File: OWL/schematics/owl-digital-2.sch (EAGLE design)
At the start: 72 parts, among them IC1 LMC6482, IC10 IS42S16400J, IC4 CS4271, IC8 STM32F756ZLQFP144, IC9 N25Q128A13, U2 1uH, U3 1uH, U4 V_REG_LM3940IMP, Y1 24.576MHz, Y3 25MHz

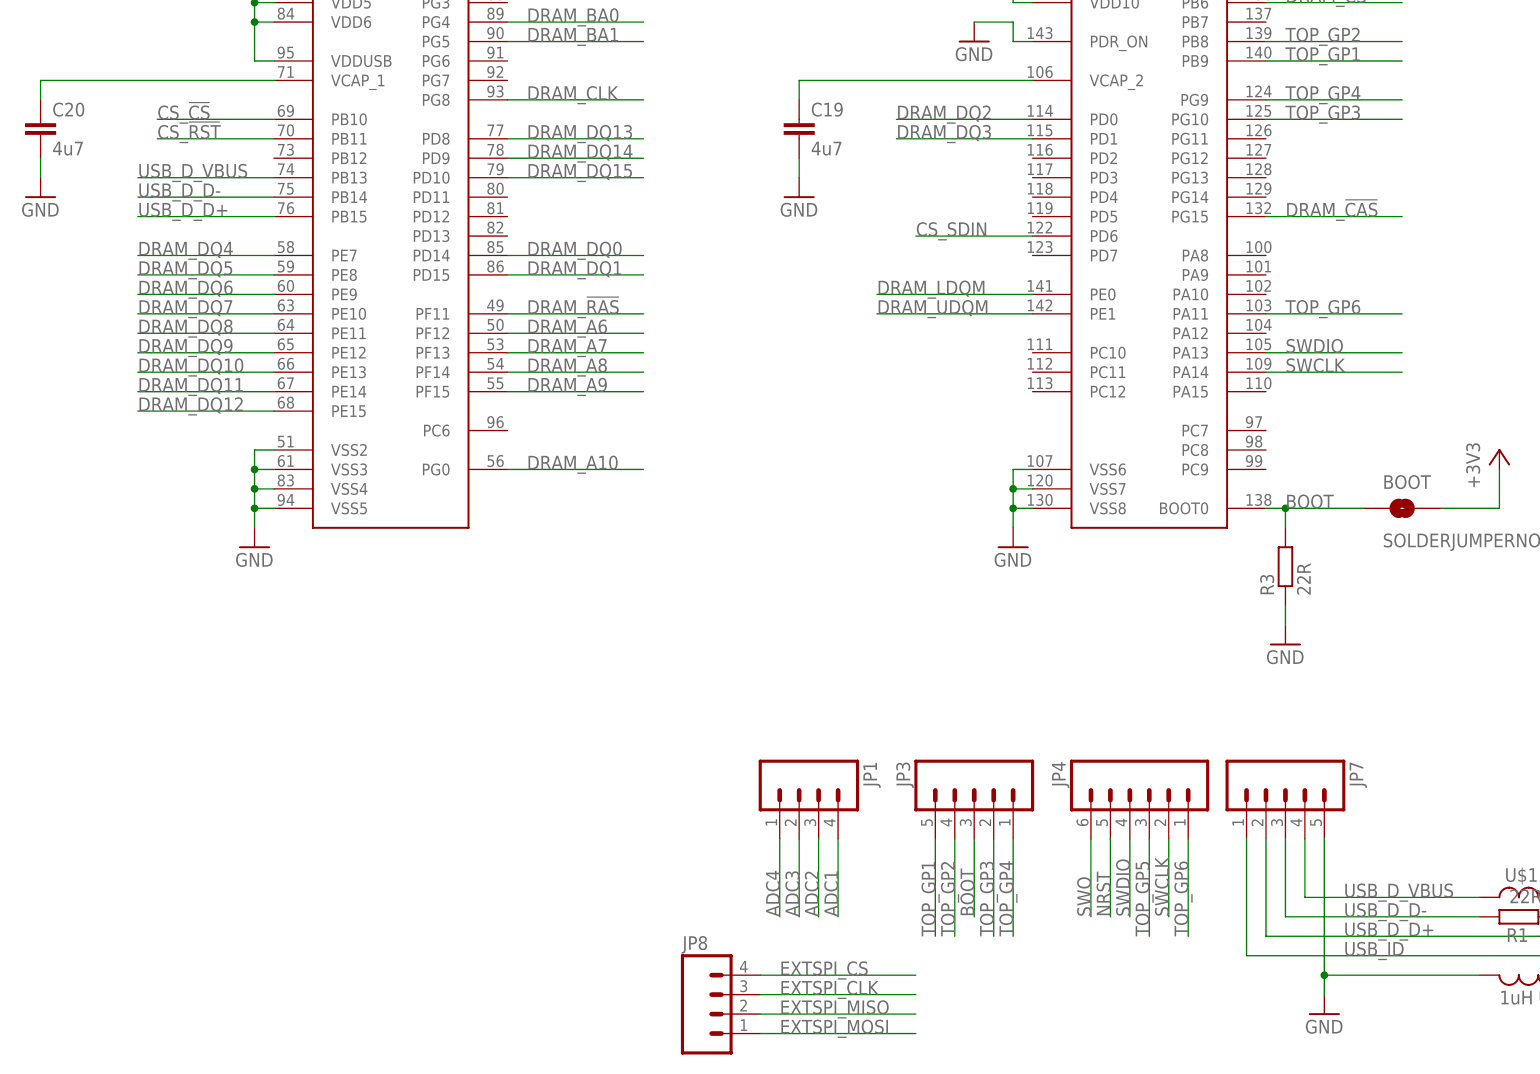
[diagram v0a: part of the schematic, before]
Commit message: updated USB ID pin on cube file and hardware
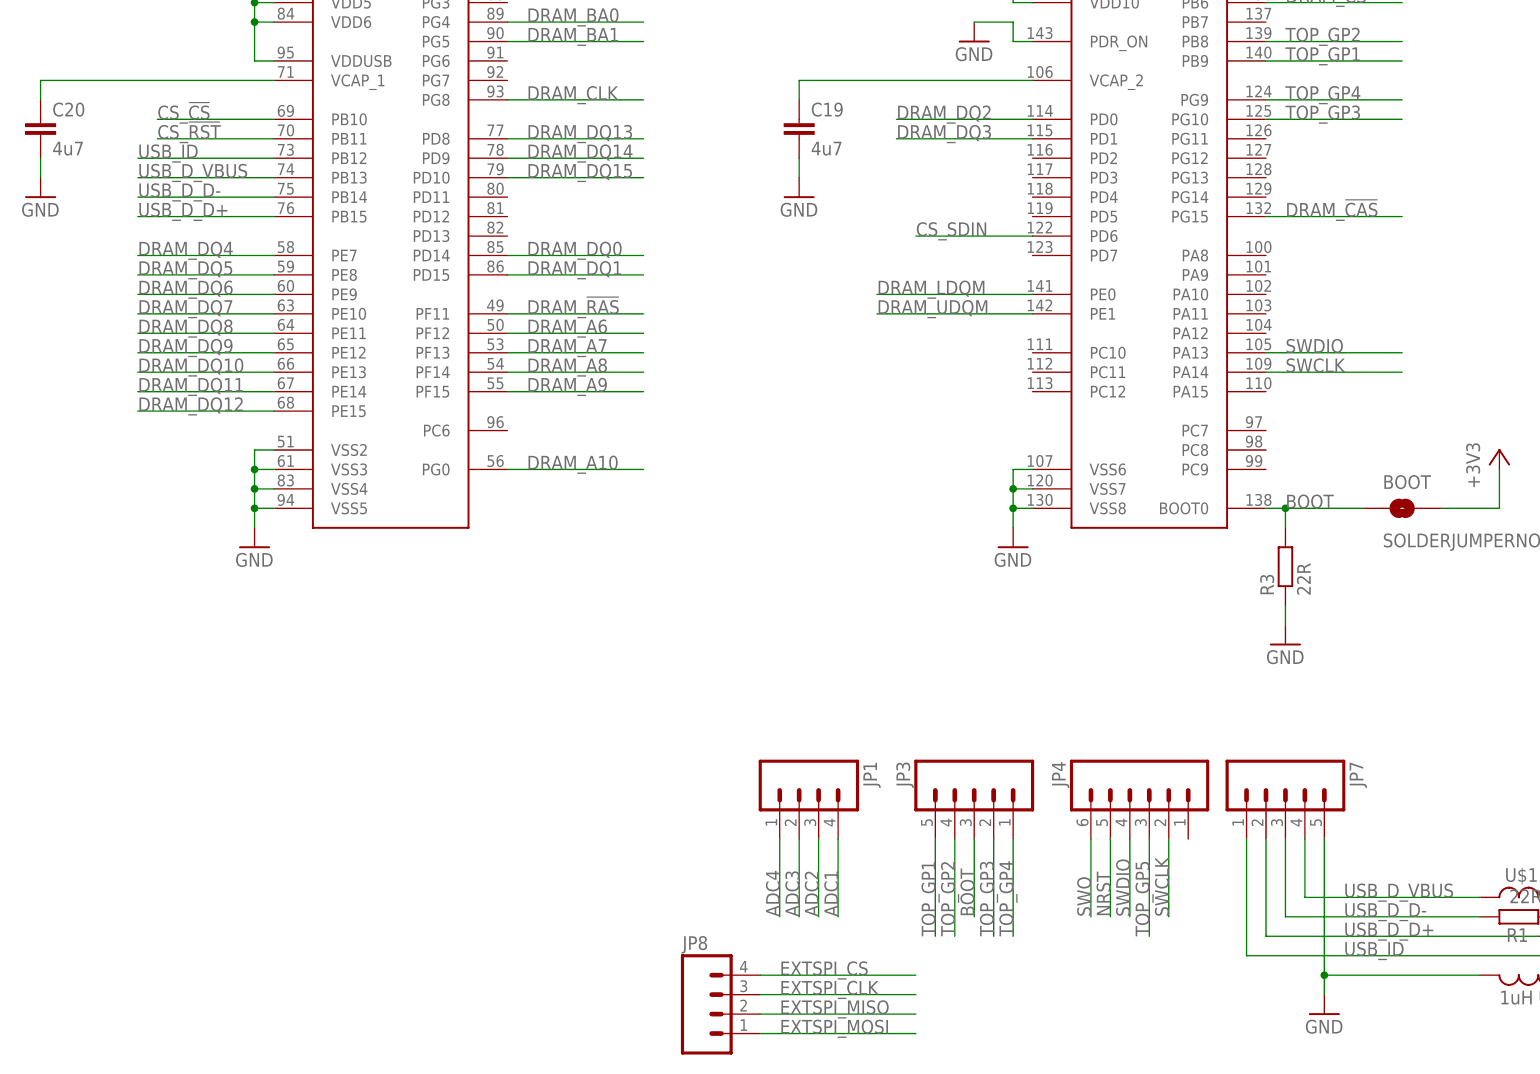
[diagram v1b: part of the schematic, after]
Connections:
- removed net TOP_GP6: IC8G$3.PA11, JP4.1
- net USB_ID: now also IC8G$2.PB12
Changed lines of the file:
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@@
 <pinref part="USB1" gate="USB" pin="ID"/>
+</segment>
+<segment>
+<pinref part="IC8" gate="G$2" pin="PB12"/>
+<wire x1="139.7" y1="119.38" x2="121.92" y2="119.38" width="0.1524" layer="91"/>
+<label x="121.92" y="119.38" size="1.778" layer="95"/>
 </segment>
 </net>
@@
 </segment>
 </net>
-<net name="TOP_GP6" class="0">
-<segment>
-<pinref part="JP4" gate="G$1" pin="1"/>
-<wire x1="259.08" y1="30.48" x2="259.08" y2="17.78" width="0.1524" layer="91"/>
-<label x="259.08" y="17.78" size="1.778" layer="95" rot="R90"/>
-</segment>
-<segment>
-<pinref part="IC8" gate="G$3" pin="PA11"/>
-<wire x1="269.24" y1="99.06" x2="287.02" y2="99.06" width="0.1524" layer="91"/>
-<label x="271.78" y="99.06" size="1.778" layer="95"/>
-</segment>
-</net>

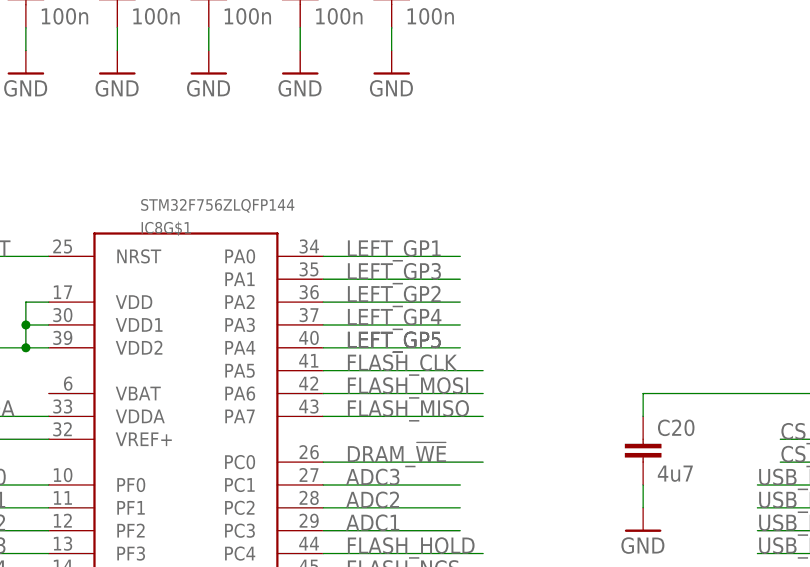
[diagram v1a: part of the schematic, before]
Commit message: Created cube file for Tesseract and swapped GP1 & GP3 pins on OWL digital v2
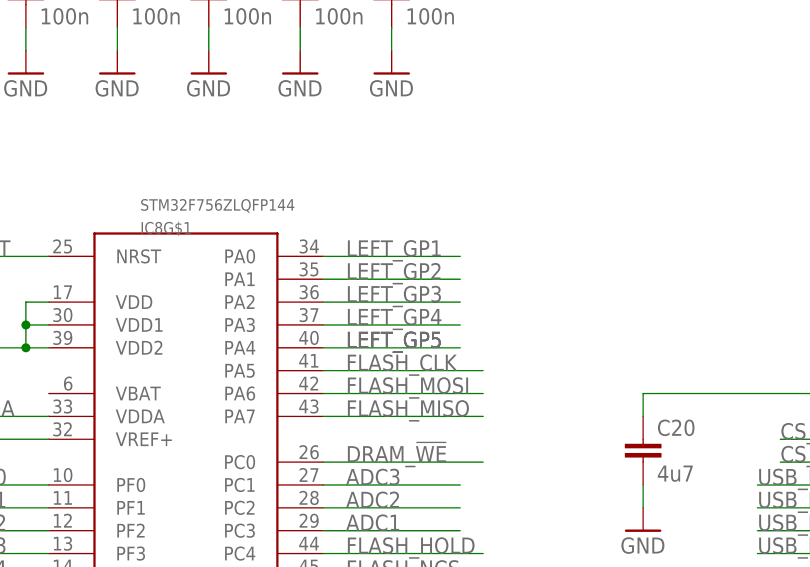
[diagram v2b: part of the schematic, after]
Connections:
- net LEFT_GP2: now also IC8G$1.PA1; no longer IC8G$1.PA2
- net LEFT_GP3: now also IC8G$1.PA2; no longer IC8G$1.PA1
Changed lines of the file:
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@@
 </segment>
 <segment>
-<pinref part="IC8" gate="G$1" pin="PA2"/>
-<wire x1="73.66" y1="139.7" x2="88.9" y2="139.7" width="0.1524" layer="91"/>
-<label x="76.2" y="139.7" size="1.778" layer="95"/>
+<pinref part="IC8" gate="G$1" pin="PA1"/>
+<wire x1="73.66" y1="142.24" x2="88.9" y2="142.24" width="0.1524" layer="91"/>
+<label x="76.2" y="142.24" size="1.778" layer="95"/>
 </segment>
 </net>
@@
 </segment>
 <segment>
-<pinref part="IC8" gate="G$1" pin="PA1"/>
-<wire x1="73.66" y1="142.24" x2="88.9" y2="142.24" width="0.1524" layer="91"/>
-<label x="76.2" y="142.24" size="1.778" layer="95"/>
+<pinref part="IC8" gate="G$1" pin="PA2"/>
+<wire x1="73.66" y1="139.7" x2="88.9" y2="139.7" width="0.1524" layer="91"/>
+<label x="76.2" y="139.7" size="1.778" layer="95"/>
 </segment>
 </net>

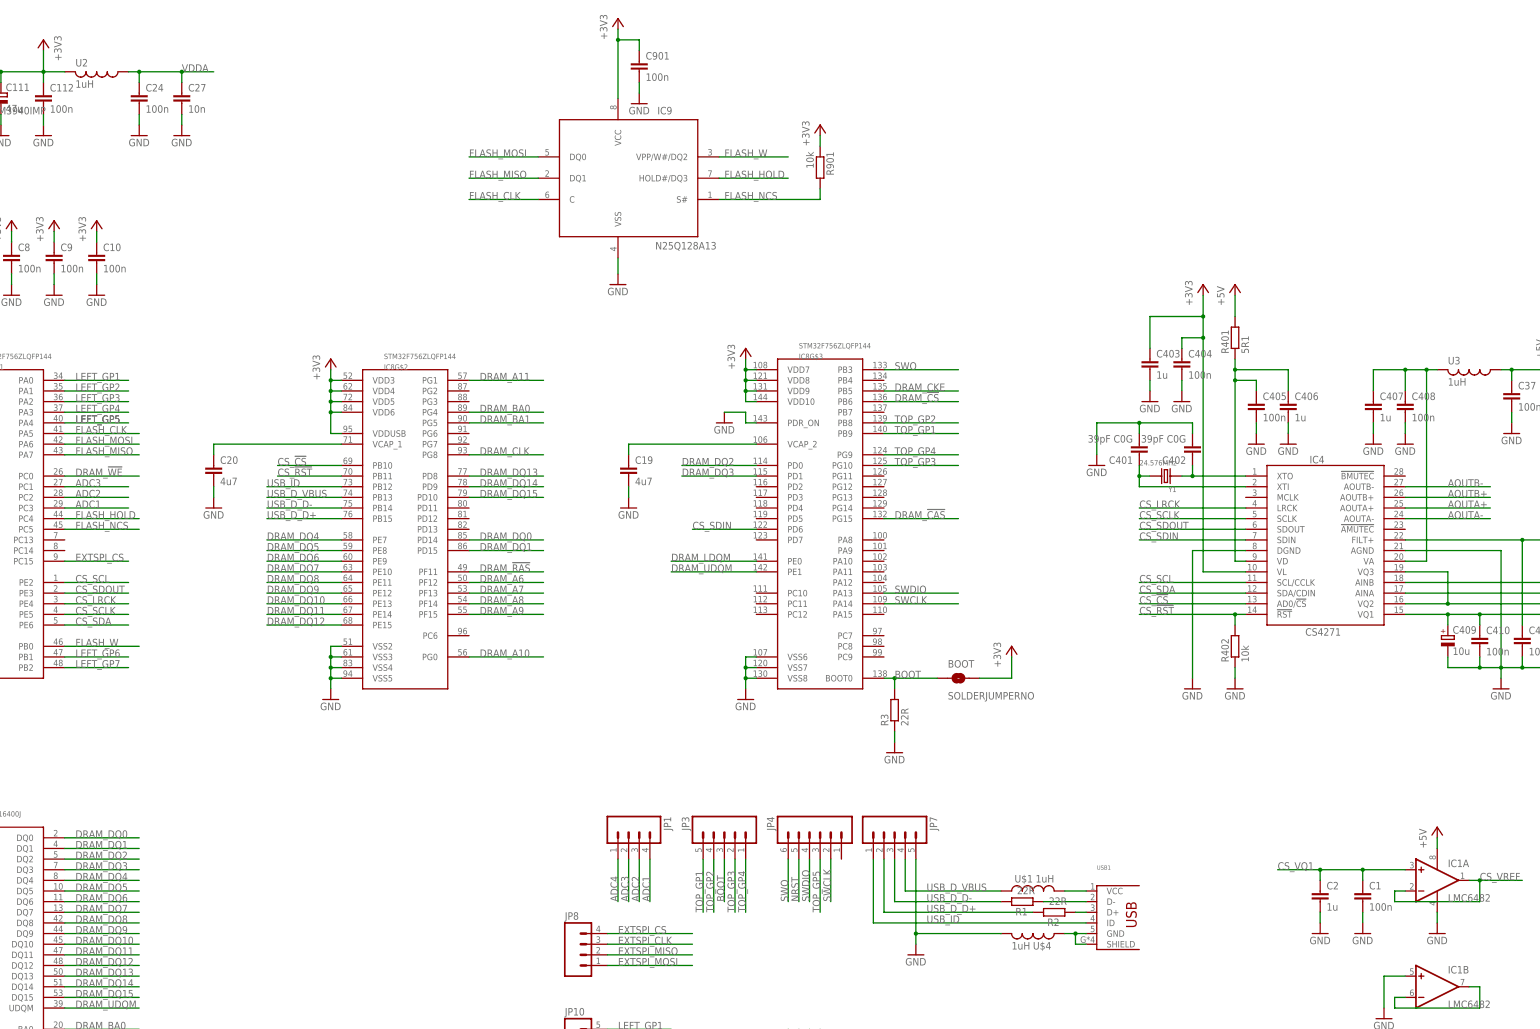
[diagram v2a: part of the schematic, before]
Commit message: changed inductor names and labels
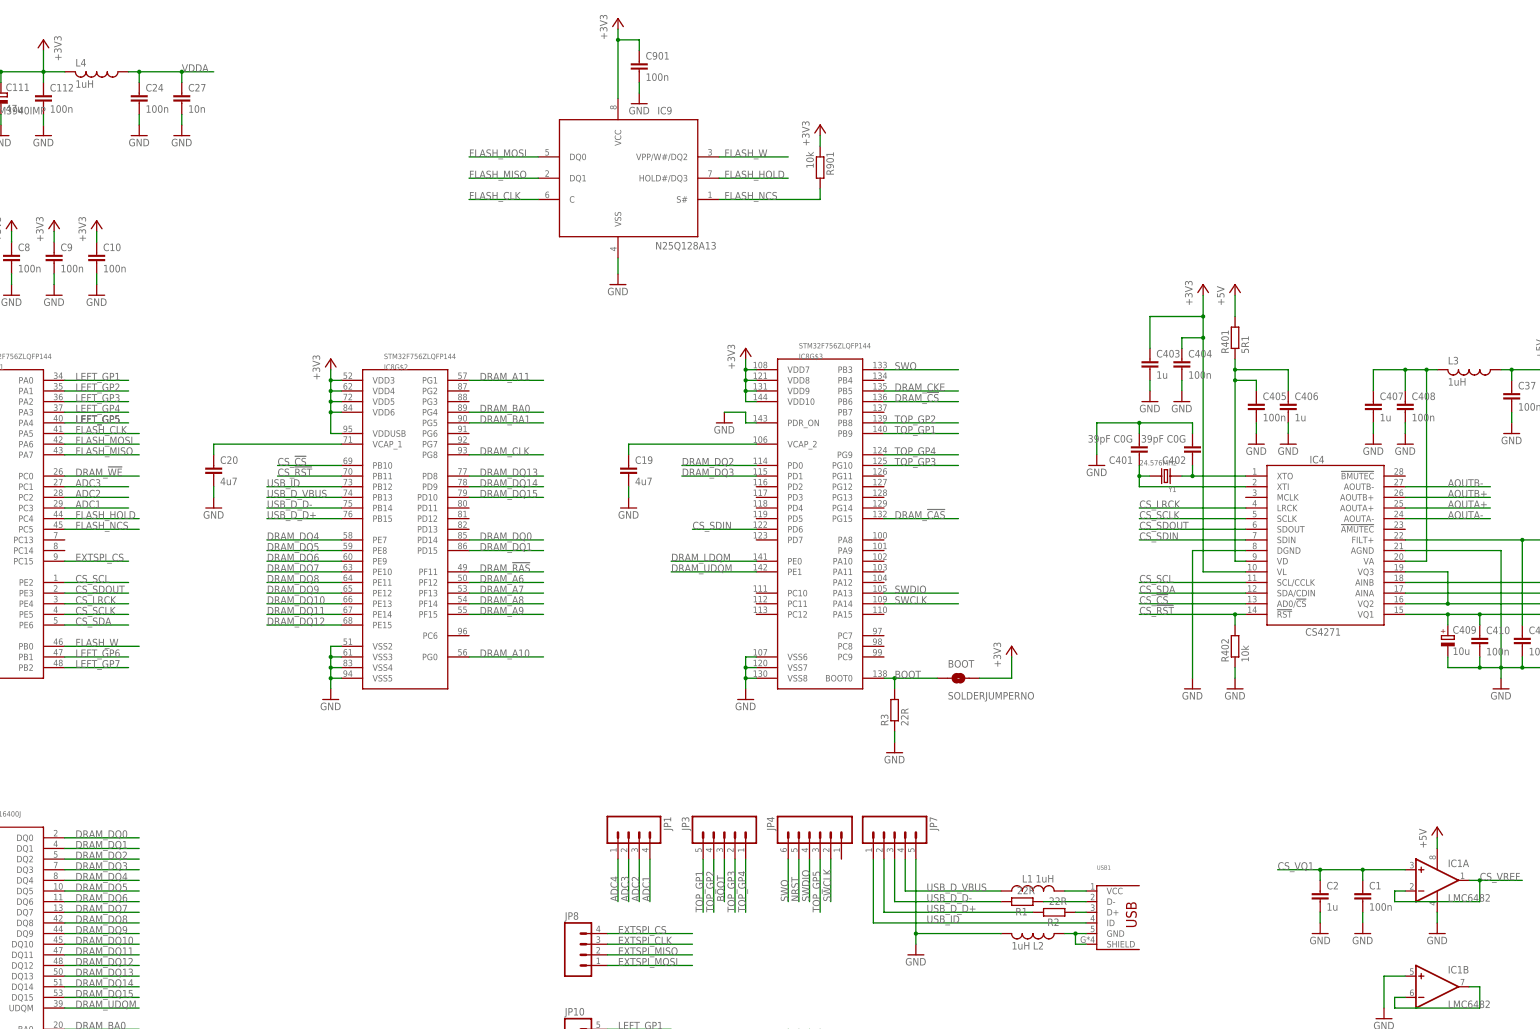
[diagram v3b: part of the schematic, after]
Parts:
- renumbered U$1 to L1, U$4 to L2, U2 to L4, U3 to L3
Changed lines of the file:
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@@
 <?xml version="1.0" encoding="utf-8"?>
 <!DOCTYPE eagle SYSTEM "eagle.dtd">
-<eagle version="6.6.0">
+<eagle version="7.5.0">
 <drawing>
 <settings>
@@
 <part name="C24" library="Rebel" deviceset="C-EU" device="C0603" value="100n"/>
 <part name="GND122" library="supply1" deviceset="GND" device=""/>
-<part name="U2" library="Rebel" deviceset="INDUCTOR" device="" value="1uH">
+<part name="L4" library="Rebel" deviceset="INDUCTOR" device="" value="1uH">
 <attribute name="OC_FARNELL" value="2288736"/>
 </part>
@@
 <part name="C37" library="Rebel" deviceset="C-EU" device="C0603" value="100n"/>
 <part name="GND6" library="supply1" deviceset="GND" device=""/>
-<part name="U3" library="Rebel" deviceset="INDUCTOR" device="" value="1uH">
+<part name="L3" library="Rebel" deviceset="INDUCTOR" device="" value="1uH">
 <attribute name="OC_FARNELL" value="2288736"/>
 </part>
@@
 <part name="+3V14" library="supply1" deviceset="+3V3" device=""/>
 <part name="GND3" library="supply1" deviceset="GND" device=""/>
-<part name="U$1" library="Rebel" deviceset="INDUCTOR" device="" value="1uH">
+<part name="L1" library="Rebel" deviceset="INDUCTOR" device="" value="1uH">
 <attribute name="OC_FARNELL" value="2288736"/>
 </part>
-<part name="U$4" library="Rebel" deviceset="INDUCTOR" device="" value="1uH">
+<part name="L2" library="Rebel" deviceset="INDUCTOR" device="" value="1uH">
 <attribute name="OC_FARNELL" value="2288736"/>
 </part>
@@
 <instance part="C24" gate="G$1" x="91.44" y="213.36"/>
 <instance part="GND122" gate="1" x="91.44" y="203.2"/>
-<instance part="U2" gate="G$1" x="81.28" y="218.44" rot="R180">
+<instance part="L4" gate="G$1" x="81.28" y="218.44" rot="R180">
 <attribute name="OC_FARNELL" x="81.28" y="218.44" size="1.778" layer="96" rot="R180" display="off"/>
 </instance>
@@
 <instance part="C37" gate="G$1" x="419.1" y="142.24"/>
 <instance part="GND6" gate="1" x="419.1" y="132.08"/>
-<instance part="U3" gate="G$1" x="408.94" y="147.32" rot="R180">
+<instance part="L3" gate="G$1" x="408.94" y="147.32" rot="R180">
 <attribute name="OC_FARNELL" x="408.94" y="147.32" size="1.778" layer="96" rot="R180" display="off"/>
 </instance>
@@
 <instance part="+3V14" gate="G$1" x="243.84" y="-22.86"/>
 <instance part="GND3" gate="1" x="241.3" y="-45.72"/>
-<instance part="U$1" gate="G$1" x="304.8" y="22.86" smashed="yes">
+<instance part="L1" gate="G$1" x="304.8" y="22.86" smashed="yes">
 <attribute name="OC_FARNELL" x="304.8" y="22.86" size="1.778" layer="96" display="off"/>
 <attribute name="NAME" x="304.8" y="26.67" size="1.778" layer="95" rot="R180"/>
 <attribute name="VALUE" x="309.88" y="26.67" size="1.778" layer="96" rot="R180"/>
 </instance>
-<instance part="U$4" gate="G$1" x="304.8" y="12.7" smashed="yes" rot="R180">
+<instance part="L2" gate="G$1" x="304.8" y="12.7" smashed="yes" rot="R180">
 <attribute name="OC_FARNELL" x="304.8" y="12.7" size="1.778" layer="96" rot="R180" display="off"/>
 <attribute name="NAME" x="304.8" y="8.89" size="1.778" layer="95"/>
@@
 <wire x1="276.86" y1="10.16" x2="276.86" y2="12.7" width="0.1524" layer="91"/>
 <junction x="276.86" y="12.7"/>
-<pinref part="U$4" gate="G$1" pin="2"/>
+<pinref part="L2" gate="G$1" pin="2"/>
 </segment>
 <segment>
@@
 <pinref part="C38" gate="G$1" pin="1"/>
 <wire x1="429.26" y1="144.78" x2="429.26" y2="147.32" width="0.1524" layer="91"/>
-<pinref part="U3" gate="G$1" pin="1"/>
+<pinref part="L3" gate="G$1" pin="1"/>
 <wire x1="416.56" y1="147.32" x2="419.1" y2="147.32" width="0.1524" layer="91"/>
 <pinref part="P+6" gate="1" pin="+5V"/>
@@
 <pinref part="JP7" gate="G$1" pin="4"/>
 <wire x1="274.32" y1="30.48" x2="274.32" y2="22.86" width="0.1524" layer="91"/>
-<pinref part="U$1" gate="G$1" pin="1"/>
+<pinref part="L1" gate="G$1" pin="1"/>
 </segment>
 </net>
@@
 <wire x1="101.6" y1="215.9" x2="101.6" y2="218.44" width="0.1524" layer="91"/>
 <wire x1="101.6" y1="218.44" x2="109.22" y2="218.44" width="0.1524" layer="91"/>
-<pinref part="U2" gate="G$1" pin="1"/>
+<pinref part="L4" gate="G$1" pin="1"/>
 <junction x="91.44" y="218.44"/>
 <junction x="101.6" y="218.44"/>
@@
 <wire x1="393.7" y1="101.6" x2="398.78" y2="101.6" width="0.1524" layer="91"/>
 <wire x1="398.78" y1="101.6" x2="398.78" y2="147.32" width="0.1524" layer="91"/>
-<pinref part="U3" gate="G$1" pin="2"/>
+<pinref part="L3" gate="G$1" pin="2"/>
 <wire x1="401.32" y1="147.32" x2="398.78" y2="147.32" width="0.1524" layer="91"/>
 <junction x="398.78" y="147.32"/>
@@
 <junction x="68.58" y="218.44"/>
 <wire x1="73.66" y1="218.44" x2="68.58" y2="218.44" width="0.1524" layer="91"/>
-<pinref part="U2" gate="G$1" pin="2"/>
+<pinref part="L4" gate="G$1" pin="2"/>
 <pinref part="U4" gate="G$1" pin="OUT"/>
 </segment>
@@
 <pinref part="USB1" gate="USB" pin="GND"/>
 <wire x1="312.42" y1="12.7" x2="314.96" y2="12.7" width="0.1524" layer="91"/>
-<pinref part="U$4" gate="G$1" pin="1"/>
+<pinref part="L2" gate="G$1" pin="1"/>
 <pinref part="USB1" gate="USB" pin="SHIELD"/>
 <wire x1="314.96" y1="12.7" x2="317.5" y2="12.7" width="0.1524" layer="91"/>
@@
 <net name="N$2" class="0">
 <segment>
-<pinref part="U$1" gate="G$1" pin="2"/>
+<pinref part="L1" gate="G$1" pin="2"/>
 <pinref part="USB1" gate="USB" pin="VCC"/>
 <wire x1="312.42" y1="22.86" x2="317.5" y2="22.86" width="0.1524" layer="91"/>
